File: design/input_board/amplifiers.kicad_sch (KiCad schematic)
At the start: 26 parts, among them IC7 MUX36D08IPW, IC8 MUX508IPW, U10 INA849DGK, U11 INA849DGK, U12 INA849DGK, U13 INA849DGK, U6 INA849DGK, U7 INA849DGK, U8 INA849DGK, U9 INA849DGK

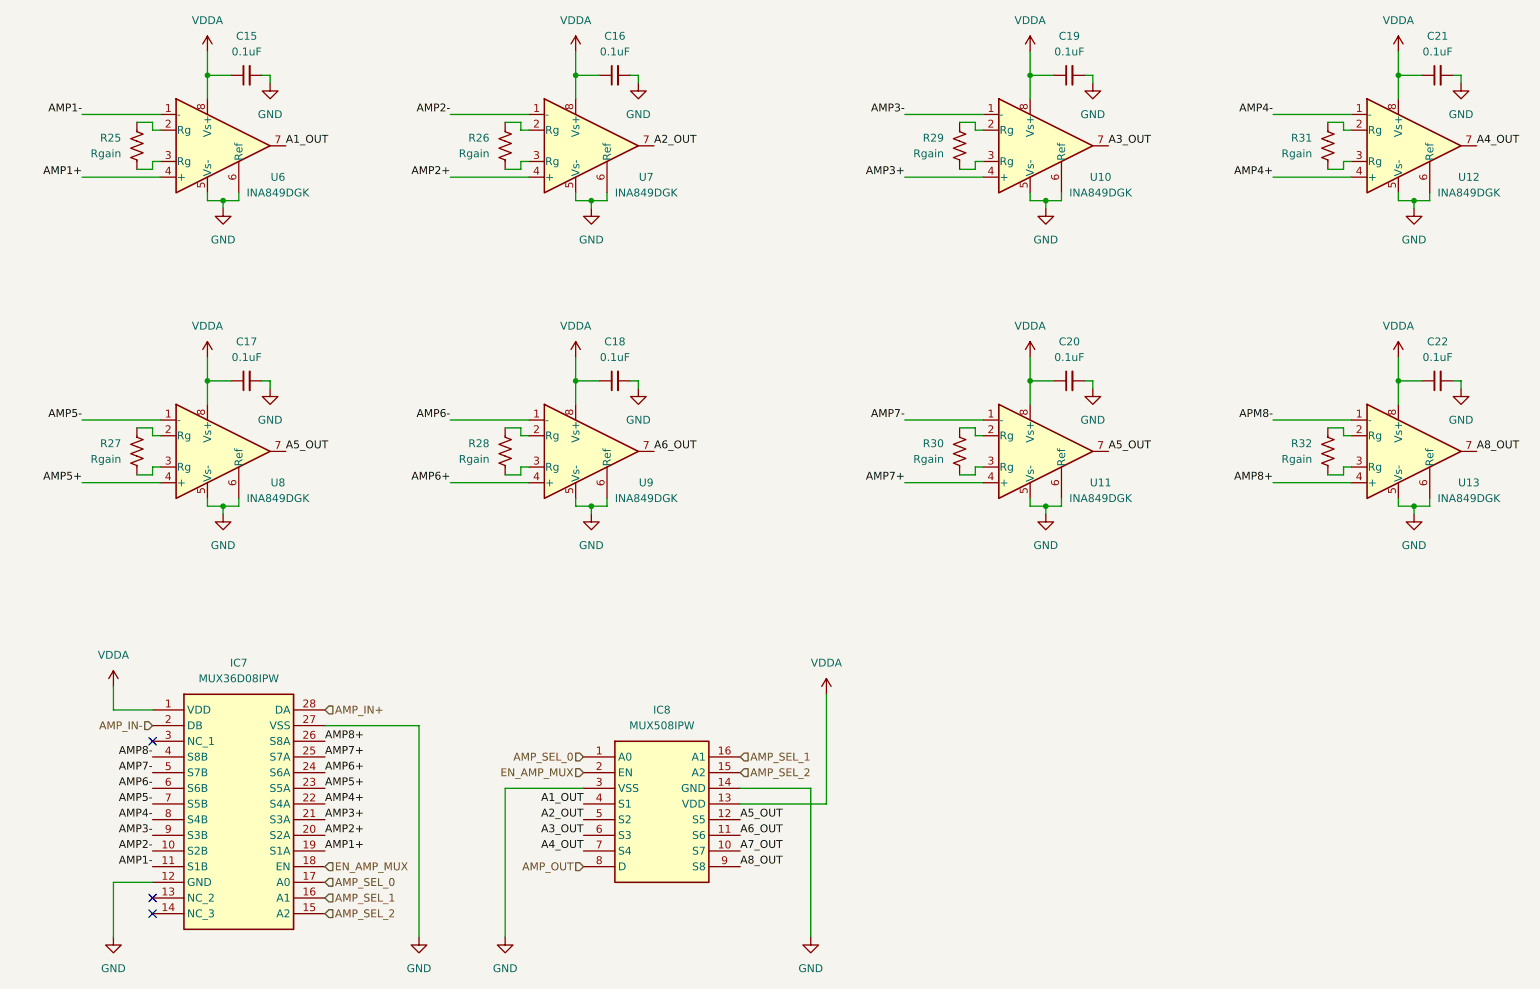
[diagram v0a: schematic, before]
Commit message: Finihs schamtic and footprints; DVDD 3.3->2V
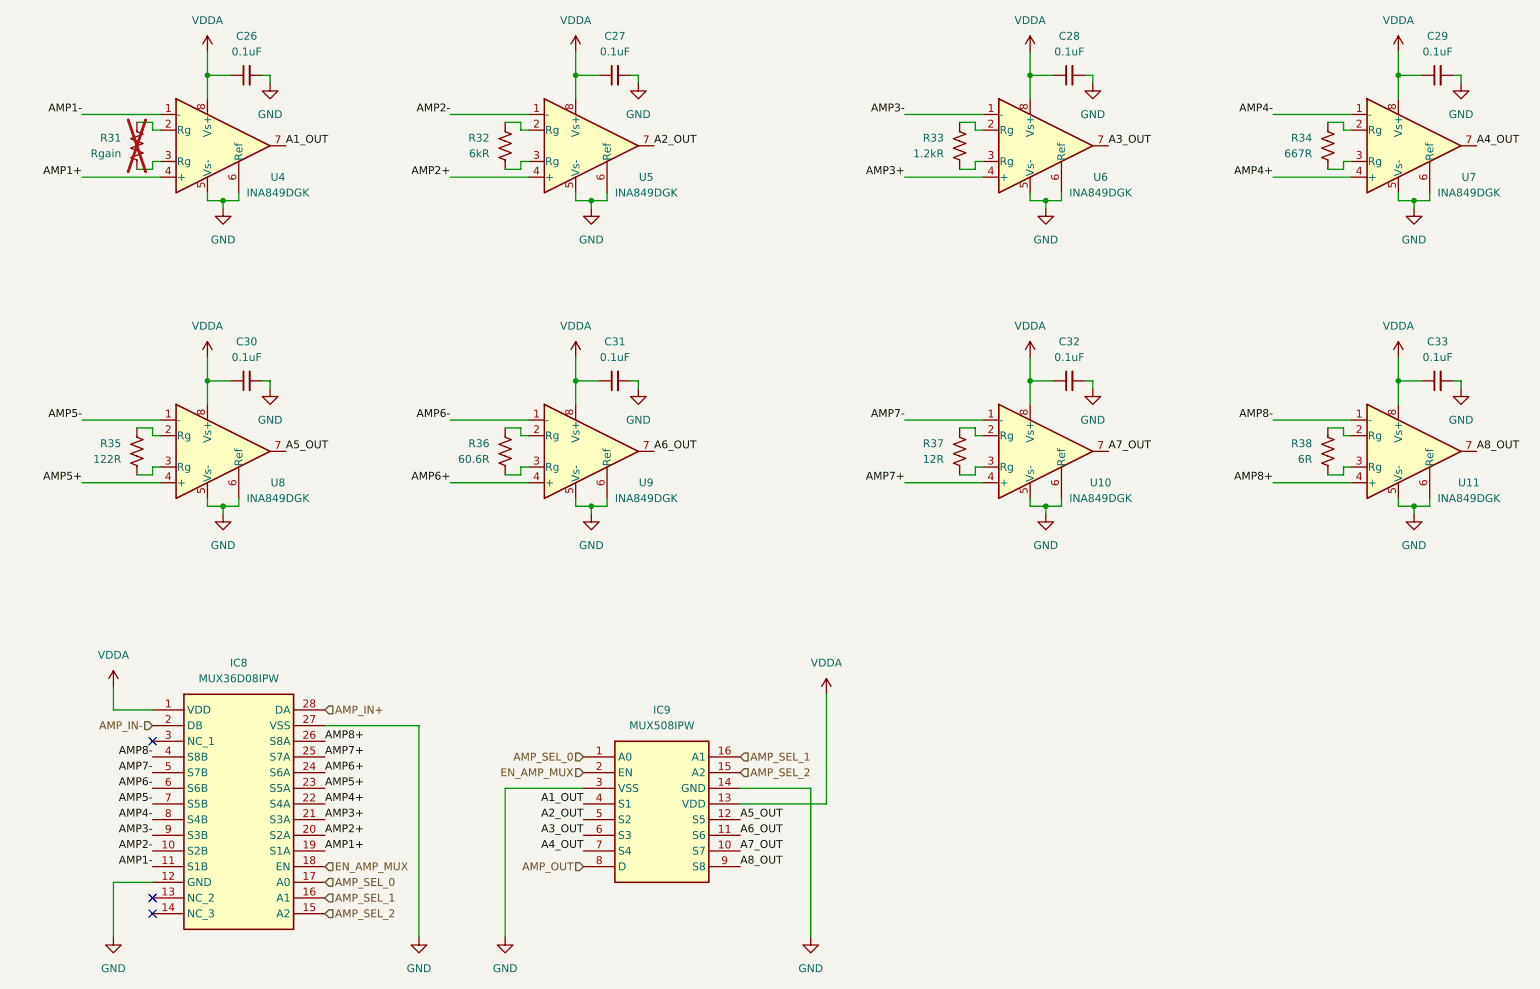
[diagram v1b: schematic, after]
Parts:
- C26: renamed from C15; footprint (none) -> Capacitor_SMD:C_0805_2012Metric_Pad1.18x1.45mm_HandSolder
- C27: renamed from C16; footprint (none) -> Capacitor_SMD:C_0805_2012Metric_Pad1.18x1.45mm_HandSolder
- C28: renamed from C19; footprint (none) -> Capacitor_SMD:C_0805_2012Metric_Pad1.18x1.45mm_HandSolder
- C29: renamed from C21; footprint (none) -> Capacitor_SMD:C_0805_2012Metric_Pad1.18x1.45mm_HandSolder
- C30: renamed from C17; footprint (none) -> Capacitor_SMD:C_0805_2012Metric_Pad1.18x1.45mm_HandSolder
- C31: renamed from C18; footprint (none) -> Capacitor_SMD:C_0805_2012Metric_Pad1.18x1.45mm_HandSolder
- C32: renamed from C20; footprint (none) -> Capacitor_SMD:C_0805_2012Metric_Pad1.18x1.45mm_HandSolder
- C33: renamed from C22; footprint (none) -> Capacitor_SMD:C_0805_2012Metric_Pad1.18x1.45mm_HandSolder
- IC8: renamed from IC7; footprint SOP65P640X120-28N -> input_board:SOP65P640X120-28N
- IC9: renamed from IC8; footprint SOP65P640X120-16N -> input_board:SOP65P640X120-16N
- R31: renamed from R25; now not fitted; now left out of the parts list
- R32: renamed from R26; value Rgain -> 6kR; footprint (none) -> Resistor_SMD:R_0805_2012Metric_Pad1.20x1.40mm_HandSolder
- R33: renamed from R29; value Rgain -> 1.2kR; footprint (none) -> Resistor_SMD:R_0805_2012Metric_Pad1.20x1.40mm_HandSolder
- R34: renamed from R31; value Rgain -> 667R; footprint (none) -> Resistor_SMD:R_0805_2012Metric_Pad1.20x1.40mm_HandSolder
- R35: renamed from R27; value Rgain -> 122R; footprint (none) -> Resistor_SMD:R_0805_2012Metric_Pad1.20x1.40mm_HandSolder
- R36: renamed from R28; value Rgain -> 60.6R; footprint (none) -> Resistor_SMD:R_0805_2012Metric_Pad1.20x1.40mm_HandSolder
- R37: renamed from R30; value Rgain -> 12R; footprint (none) -> Resistor_SMD:R_0805_2012Metric_Pad1.20x1.40mm_HandSolder
- R38: renamed from R32; value Rgain -> 6R; footprint (none) -> Resistor_SMD:R_0805_2012Metric_Pad1.20x1.40mm_HandSolder
- renumbered U11 to U10, U13 to U11, U6 to U4, U7 to U5, U10 to U6, U12 to U7
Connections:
- net APM8- is gone; now on net AMP8-: U11.1 (-)
- net A5_OUT: no longer U10.7
- net A7_OUT: now also U10.7

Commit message: Layout v2; better
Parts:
- added C70, C71: 0.1uF, Capacitor_SMD:C_0805_2012Metric_Pad1.18x1.45mm_HandSolder, symbol Device:C
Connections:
- net GND: now also C70.1, C71.1
- net VDDA: now also C70.2, C71.2
